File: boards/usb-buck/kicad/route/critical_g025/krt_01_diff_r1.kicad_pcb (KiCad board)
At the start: 4 copper layers, 50 x 40 mm, 28 parts, among them J1 USB Micro-B receptacle SMD, J2 1x4 2.54mm male THT, SW1 SMD tactile switch, U1 STM32F103C8T6, U2 AP63203QWU-7, U3 USBLC6-2SC6, Y1 8MHz 20pF

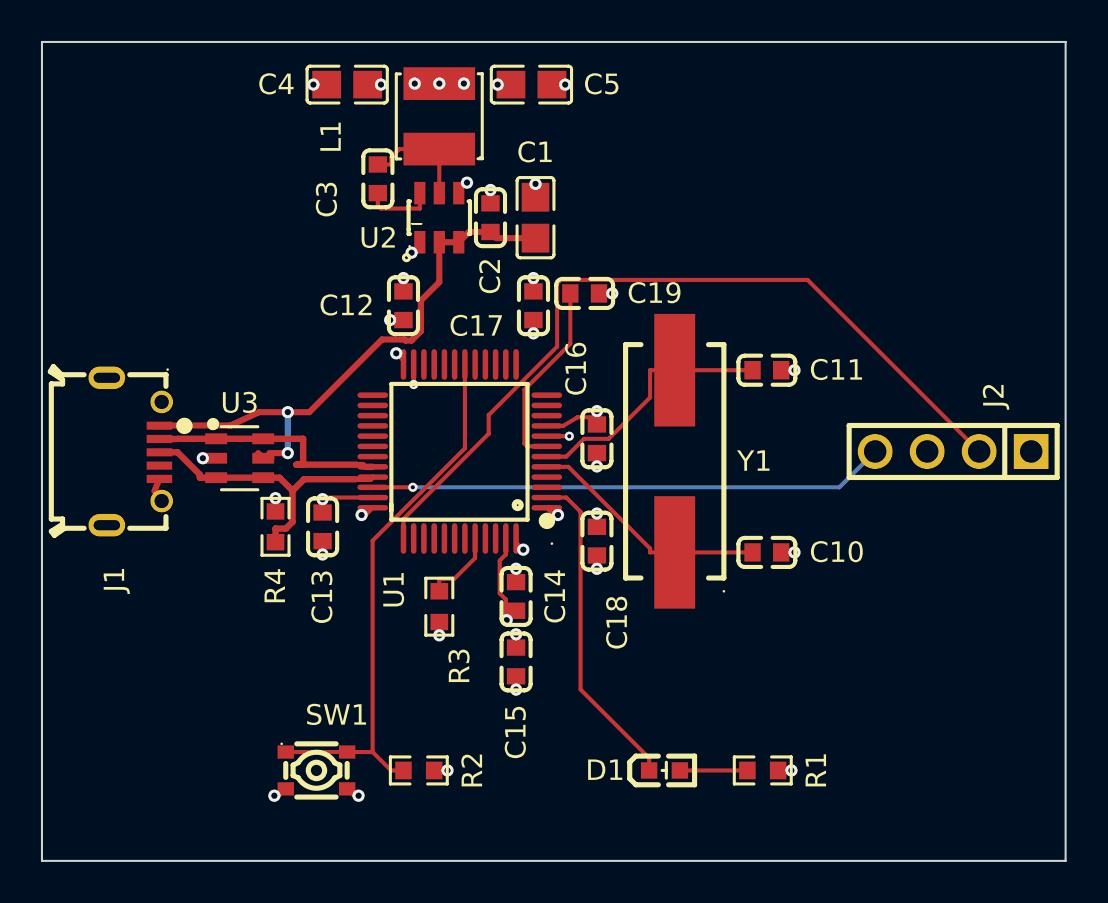
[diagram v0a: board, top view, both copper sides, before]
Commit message: ai-ee usb-buck: drc_routed pass (4L chain; 4 router-found defects fixed in-run)
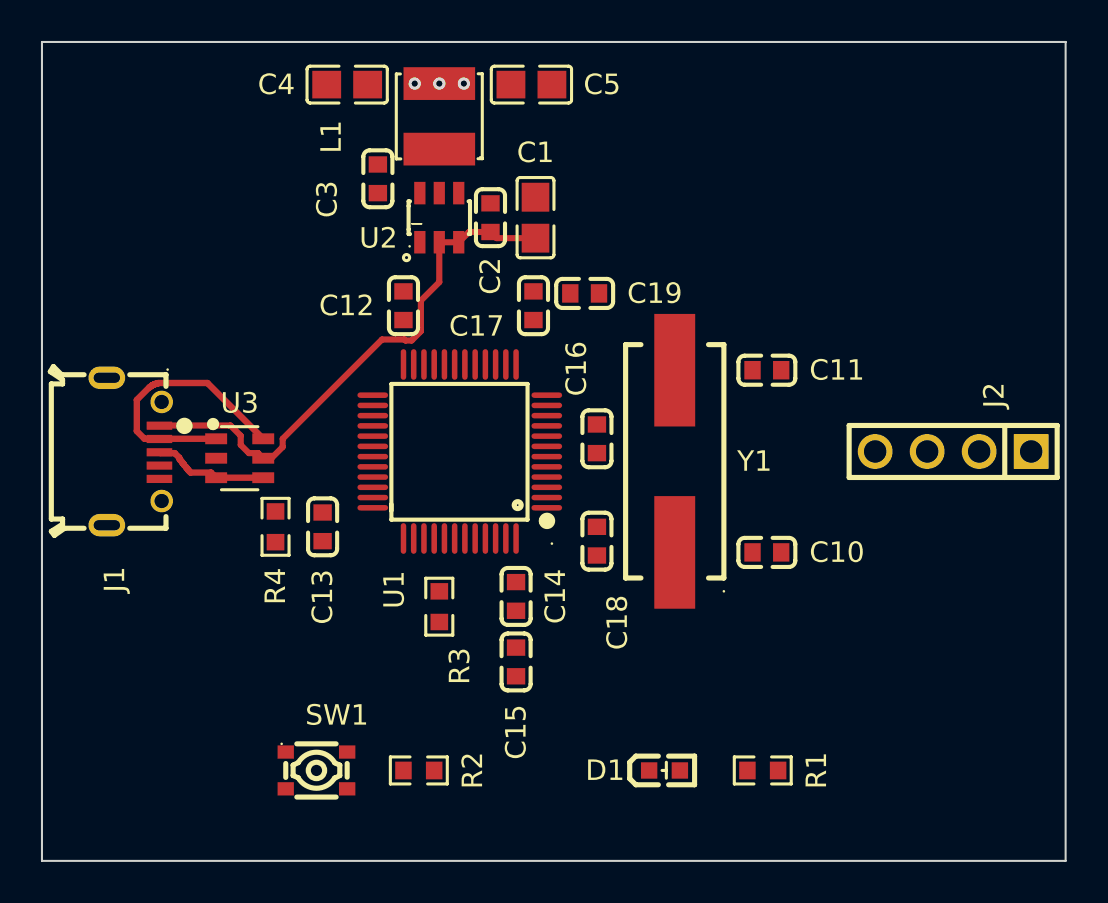
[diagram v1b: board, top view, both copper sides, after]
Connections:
- R4 pad 1: /USB_DP -> (no net)
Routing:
- net /mcu/SWCLK: track 39.7 -> 0.00 mm
- net GND: track 29.8 -> 0.00 mm, vias 21 -> 0
- net /mcu/BTN: track 26.9 -> 0.00 mm
- net /mcu/SWDIO: track 25.3 -> 0.00 mm, vias 1 -> 0
- net +3V3: track 16.8 -> 0.00 mm, vias 20 -> 3
- net /mcu/LED: track 16.0 -> 0.00 mm
- net /mcu/OSC_OUT: track 12.6 -> 0.00 mm
- net /mcu/OSC_IN: track 11.9 -> 0.00 mm
- net /mcu/NRST: track 9.41 -> 0.00 mm
- net /USB_DP: track 14.7 -> 5.71 mm
- net /power/SW: track 5.67 -> 0.00 mm
- net /mcu/BOOT0: track 3.73 -> 0.00 mm
- net /power/BST: track 3.47 -> 0.00 mm
- net /mcu/LED_A: track 3.30 -> 0.00 mm
- net VBUS: track 28.0 -> 26.3 mm, vias 2 -> 0
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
